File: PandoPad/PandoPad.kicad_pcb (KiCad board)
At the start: 2 copper layers, 90 parts, among them J1 78171-0004, J2 Conn_01x05, J3 MalePogo, J4 FemalePogo, K1 Num, K10 8, K11 9, K12 Right+, K13 4, K14 5, K15 6, K16 OPT2, K17 1, K18 2, K19 3, K2 /, K20 REnt, K22 LZero, K23 ., K24 ., K25 OPT5, K3 *, K4 -, K9 7, P1 OLED1, P2 OLED2, P3 OLED2, SW1 Mod1, SW2 Mod2, SW3 Mod3, SW4 Mod4, SW5 SW_Push, U1 W25Q128JVS, U2 XC6206PxxxMR-Regulator_Linear, U3 RP2040, Y1 12MHz

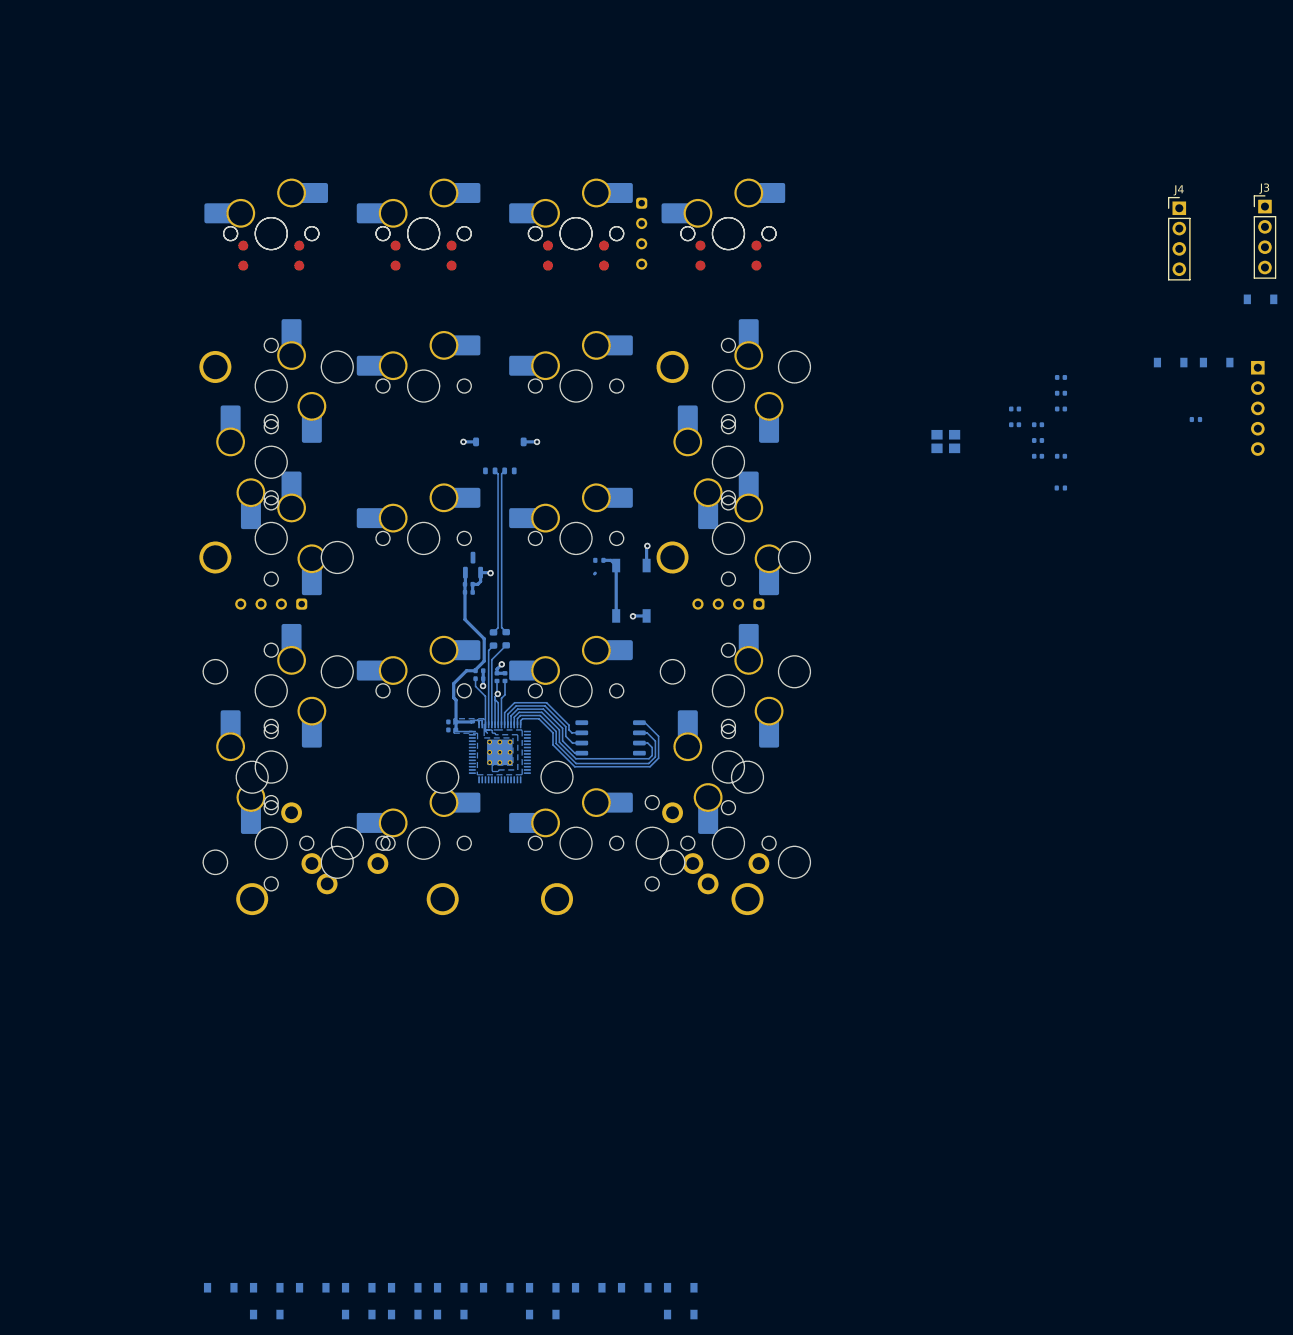
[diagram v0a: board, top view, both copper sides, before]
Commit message: Finished Routing
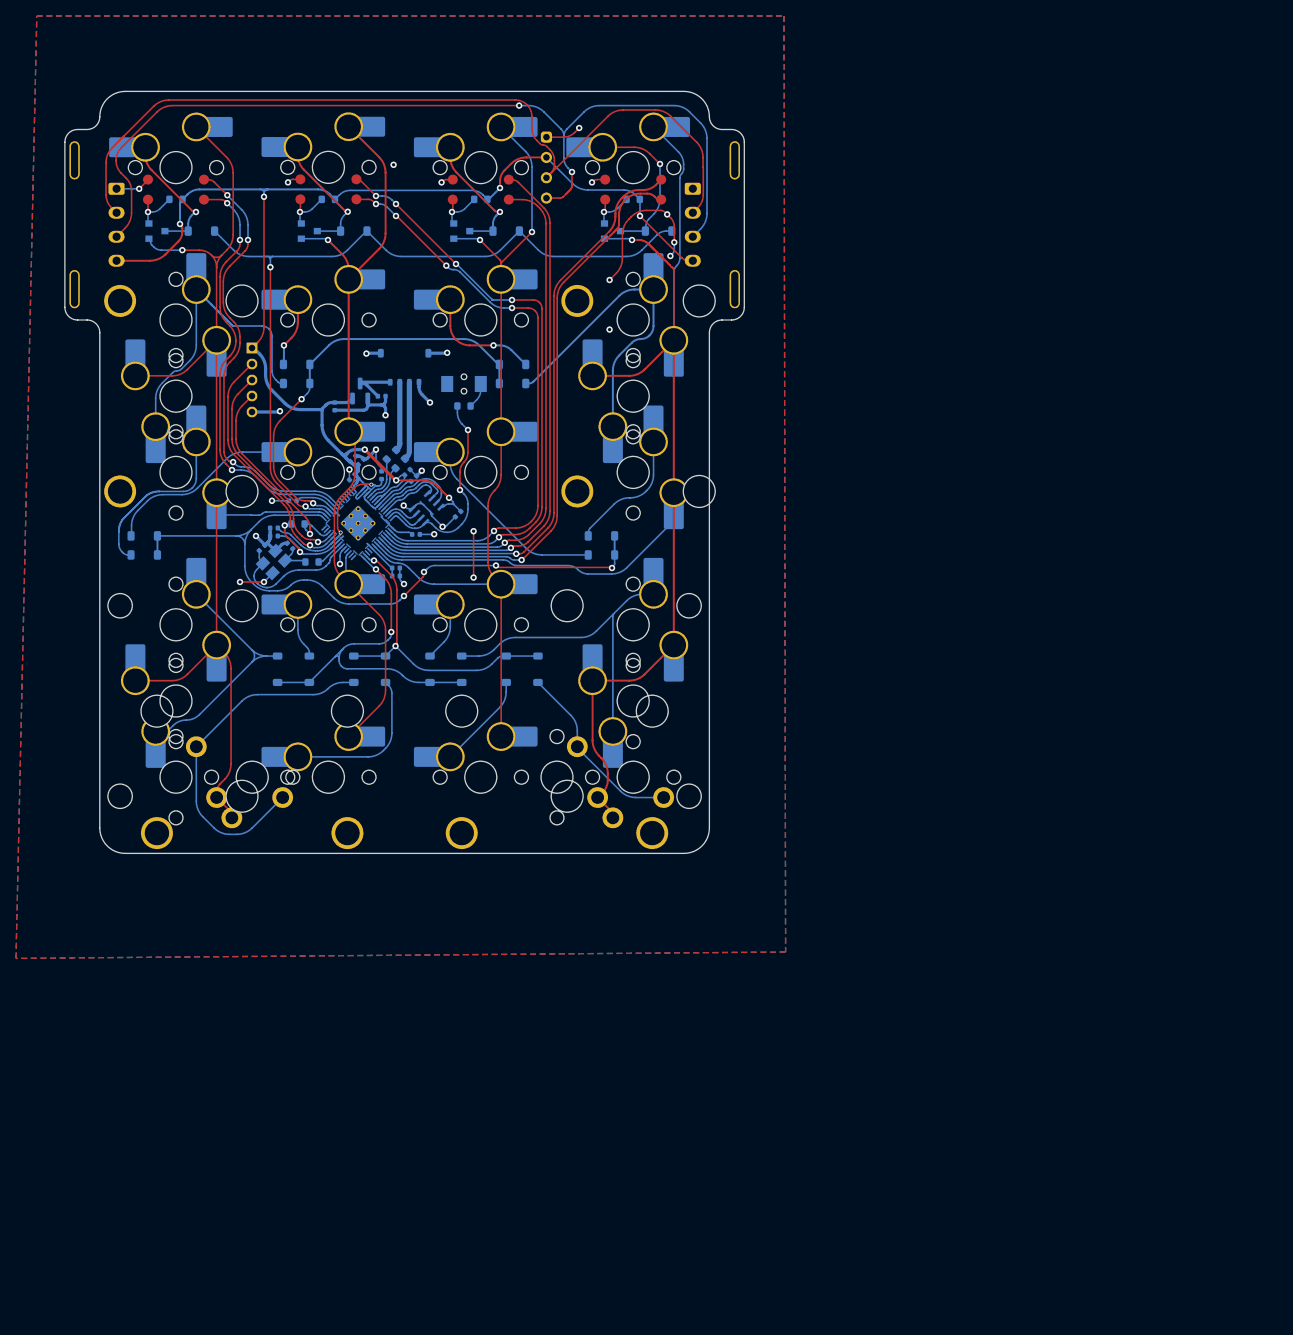
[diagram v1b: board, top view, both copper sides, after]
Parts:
- removed C1: 100nF, Capacitor_SMD:C_0402_1005Metric
- removed P2, P3: OLED2, Libraries:OLED_v2
- removed SW1: Mod1, Switch_Keyboard_Hotswap_Kailh:SW_Hotswap_Kailh_MX_plated_1.00u_Enc_Standalone
- removed SW2: Mod2, Switch_Keyboard_Hotswap_Kailh:SW_Hotswap_Kailh_MX_plated_1.00u_Enc_Standalone
- removed SW3: Mod3, Switch_Keyboard_Hotswap_Kailh:SW_Hotswap_Kailh_MX_plated_1.00u_Enc_Standalone
- removed SW4: Mod4, Switch_Keyboard_Hotswap_Kailh:SW_Hotswap_Kailh_MX_plated_1.00u_Enc_Standalone
- removed U1: W25Q128JVS, Package_SO:SOIC-8_5.23x5.23mm_P1.27mm
- added C18: 100nF, Capacitor_SMD:C_0402_1005Metric, B.Cu at (127.3, 90.6)
- added Q1: PMOS, Keebio-Parts:SOT-23, B.Cu at (89.7, 55.2)
- added Q2: PMOS, Keebio-Parts:SOT-23, B.Cu at (108.7, 55.2)
- added Q3: PMOS, Keebio-Parts:SOT-23, B.Cu at (127.8, 55.2)
- added Q4: PMOS, Keebio-Parts:SOT-23, B.Cu at (146.6, 55.2)
- added R6: 1k, Resistor_SMD:R_0603_1608Metric, B.Cu at (92.1, 51.3)
- added R7: 1k, Resistor_SMD:R_0603_1608Metric, B.Cu at (111.1, 51.3)
- added R8: 1k, Resistor_SMD:R_0603_1608Metric, B.Cu at (130.2, 51.3)
- added R9: 1k, Resistor_SMD:R_0603_1608Metric, B.Cu at (149.2, 51.3)
- added U4: W25Q32JVUUIQ, Extra-components:SON80P400X300X60-10N, B.Cu at (123.4, 89.9)
- J2: footprint Connector_PinSocket_2.54mm:PinSocket_1x05_P2.54mm_Vertical -> Connector_PinHeader_2.00mm:PinHeader_1x05_P2.00mm_Vertical
- J3: footprint Connector_PinHeader_2.54mm:PinHeader_1x04_P2.54mm_Vertical -> Extra-components:1x04_3.00mm_Magnetic Pogo_Male
- J4: footprint Connector_PinHeader_2.54mm:PinHeader_1x04_P2.54mm_Vertical -> Extra-components:1x04_3.00mm_Magnetic Pogo_Female
- K1: value Num -> ~; footprint Switch_Keyboard_Hotswap_Kailh:SW_Hotswap_Kailh_MX_plated_1.00u_Vias -> Switch_Keyboard_Hotswap_Kailh:SW_Hotswap_Kailh_MX_plated_1.00u_Enc_Standalone
- K2: value / -> ~; footprint Switch_Keyboard_Hotswap_Kailh:SW_Hotswap_Kailh_MX_plated_1.00u_Vias -> Switch_Keyboard_Hotswap_Kailh:SW_Hotswap_Kailh_MX_plated_1.00u_Enc_Standalone
- K3: value * -> ~; footprint Switch_Keyboard_Hotswap_Kailh:SW_Hotswap_Kailh_MX_plated_1.00u_Vias -> Switch_Keyboard_Hotswap_Kailh:SW_Hotswap_Kailh_MX_plated_1.00u_Enc_Standalone
- K4: value - -> ~; footprint Switch_Keyboard_Hotswap_Kailh:SW_Hotswap_Kailh_MX_plated_1.00u_Vias -> Switch_Keyboard_Hotswap_Kailh:SW_Hotswap_Kailh_MX_plated_1.00u_Enc_Standalone
- P1: value OLED1 -> OLED2
- R1, R2, R3: footprint Resistor_SMD:R_0402_1005Metric -> Resistor_SMD:R_0603_1608Metric
- SW5: footprint Keebio-Parts:SW_SPST_TL3342 -> marbastlib-various:SW_C843666
- moved J3 143.6 mm to (84.6, 54.5)
- moved D1 138.8 mm to (95.2, 55.2)
- moved D3 138.7 mm to (133.3, 55.2)
- moved D13 136.2 mm to (88.1, 95.7)
- moved J2 125.8 mm to (101.6, 69.9)
- moved D9 116.6 mm to (107.2, 74.3)
- moved D11 115.8 mm to (134.1, 71.9), turned to 0 degrees
- moved D10 115.8 mm to (107.2, 71.9)
- moved D12 114.7 mm to (134.1, 74.3), turned to 0 degrees
- moved R2 113.0 mm to (107.3, 91.9), turned to 0 degrees
- moved D2 103.4 mm to (114.3, 55.2)
- moved C2 101.7 mm to (102.8, 94.9), turned to -135 degrees
- moved D14 99.5 mm to (88.1, 93.3)
- moved C6 98.8 mm to (104.3, 92.4)
- moved C3 97.9 mm to (106.3, 94.6), turned to -45 degrees
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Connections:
- D10 pad 1: row2 -> row1
- D11 pad 1: row2 -> row1
- D12 pad 1: row2 -> row1
- D13 pad 1: row3 -> row2
- D14 pad 1: row3 -> row2
- D15 pad 1: row3 -> row2
- D16 pad 1: row3 -> row2
- D17 pad 1: row4 -> row3
- D18 pad 1: row4 -> row3
- D19 pad 1: row4 -> row3
- D20 pad 1: row4 -> row3
- D21 pad 1: row5 -> row4
- D22 pad 1: row5 -> row4
- D23 pad 1: row5 -> row4
- D24 pad 1: row5 -> row4
- D9 pad 1: row2 -> row1
- J2 pad 1: ~{RESET} -> +3V3
- J2 pad 2: +3V3 -> SWCLK
- J2 pad 3: GND -> SWD
- J2 pad 4: SWD -> ~{RESET}
- J2 pad 5: SWCLK -> GND
- J3 pad 1: GND -> +3V3
- J3 pad 4: +3V3 -> GND
- J4 pad 1: GND -> +3V3
- J4 pad 4: +3V3 -> GND
- K1 pad 1: Net-(D1-A) -> col0
- K1 pad 2: Net-(K1-Pad2) -> Net-(D1-A)
- K10 pad 2: Net-(K10-Pad2) -> col1
- K11 pad 2: Net-(K11-Pad2) -> col2
- K12 pad 2: Net-(K12-Pad2) -> col3
- K13 pad 2: Net-(K1-Pad2) -> col0
- K14 pad 2: Net-(K10-Pad2) -> col1
- K15 pad 2: Net-(K11-Pad2) -> col2
- K16 pad 2: Net-(K12-Pad2) -> col3
- K17 pad 2: Net-(K1-Pad2) -> col0
- K18 pad 2: Net-(K10-Pad2) -> col1
- K19 pad 2: Net-(K11-Pad2) -> col2
- K2 pad 1: Net-(D2-A) -> col1
- K2 pad 2: Net-(K10-Pad2) -> Net-(D2-A)
- K20 pad 2: Net-(K12-Pad2) -> col3
- K22 pad 2: Net-(K1-Pad2) -> col0
- K23 pad 2: Net-(K10-Pad2) -> col1
- K24 pad 2: Net-(K11-Pad2) -> col2
- K25 pad 2: Net-(K12-Pad2) -> col3
- K3 pad 1: Net-(D3-A) -> col2
- K3 pad 2: Net-(K11-Pad2) -> Net-(D3-A)
- K4 pad 1: Net-(D4-A) -> col3
- K4 pad 2: Net-(K12-Pad2) -> Net-(D4-A)
- K9 pad 2: Net-(K1-Pad2) -> col0
- KO-1 pad 2: Net-(K1-Pad2) -> col0
- KO-2 pad 2: Net-(K12-Pad2) -> col3
- KO-3 pad 2: Net-(K1-Pad2) -> col0
- KO-4 pad 2: Net-(K12-Pad2) -> col3
- KO-5 pad 2: Net-(K1-Pad2) -> col0
- KO-6 pad 2: Net-(K12-Pad2) -> col3
- U3 pad 11: /GPIO8 -> unconnected-(U3-GPIO8-Pad11)
- U3 pad 12: /GPIO9 -> unconnected-(U3-GPIO9-Pad12)
- U3 pad 13: /GPIO10 -> row4
- U3 pad 14: /GPIO11 -> row3
- U3 pad 15: /GPIO12 -> unconnected-(U3-GPIO12-Pad15)
- U3 pad 16: /GPIO13 -> unconnected-(U3-GPIO13-Pad16)
- U3 pad 17: /GPIO14 -> col1
- U3 pad 18: /GPIO15 -> unconnected-(U3-GPIO15-Pad18)
- U3 pad 2: /GPIO0 -> E2A
- U3 pad 27: /GPIO16 -> unconnected-(U3-GPIO16-Pad27)
- U3 pad 28: /GPIO17 -> unconnected-(U3-GPIO17-Pad28)
- U3 pad 29: /GPIO18 -> row2
- U3 pad 3: /GPIO1 -> E2B
- U3 pad 30: /GPIO19 -> col0
- U3 pad 31: /GPIO20 -> row0
- U3 pad 32: /GPIO21 -> row1
- U3 pad 34: /GPIO22 -> E1A
- U3 pad 35: /GPIO23 -> E1B
- U3 pad 36: /GPIO24 -> unconnected-(U3-GPIO24-Pad36)
- U3 pad 37: /GPIO25 -> unconnected-(U3-GPIO25-Pad37)
- U3 pad 38: /GPIO26 -> unconnected-(U3-GPIO26/ADC0-Pad38)
- U3 pad 39: /GPIO27 -> unconnected-(U3-GPIO27/ADC1-Pad39)
- U3 pad 4: /GPIO2 -> E3A
- U3 pad 40: /GPIO28 -> unconnected-(U3-GPIO28/ADC2-Pad40)
- U3 pad 41: /GPIO29 -> unconnected-(U3-GPIO29/ADC3-Pad41)
- U3 pad 5: /GPIO3 -> E3B
- U3 pad 6: /GPIO4 -> E4B
- U3 pad 7: /GPIO5 -> E4A
- U3 pad 8: /GPIO6 -> col3
- U3 pad 9: /GPIO7 -> col2
- Y1 pad 1: /XTAL_O -> XTAL_IN
- Y1 pad 3: XTAL_IN -> /XTAL_O
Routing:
- net col3: track 0.00 -> 174.5 mm, vias 0 -> 1
- net +3V3: track 38.5 -> 206.3 mm, vias 1 -> 9
- net col0: track 0.00 -> 134.4 mm, vias 0 -> 1
- net SDA: track 0.00 -> 117.9 mm, vias 0 -> 2
- net SCL: track 0.00 -> 107.2 mm
- net row0: track 0.00 -> 101.2 mm, vias 0 -> 2
- net col2: track 0.00 -> 100.2 mm, vias 0 -> 2
- net col1: track 0.00 -> 91.7 mm, vias 0 -> 1
- net row2: track 0.00 -> 85.5 mm, vias 0 -> 4
- net GND: track 16.3 -> 97.5 mm, vias 7 -> 30
- net E2B: track 0.00 -> 76.3 mm, vias 0 -> 5
- net E2A: track 0.00 -> 73.2 mm, vias 0 -> 5
- net E4A: track 0.00 -> 73.1 mm, vias 0 -> 1
- net E4B: track 0.00 -> 72.9 mm, vias 0 -> 1
- net E3B: track 0.00 -> 67.2 mm, vias 0 -> 1
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- added copper zone on B.Cu, net GND
- added copper zone on F.Cu, net GND
- removed copper zone on B.Cu, net +1V1
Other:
- board outline added: 84.9 x 95.2 mm
